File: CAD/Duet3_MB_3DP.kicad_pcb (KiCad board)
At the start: 4 copper layers, 101.9 x 125 mm, 286 parts, among them J1 SWD, J16 EXPANSION, J17 ESP_DB, J19 A2543WV-5P, J2 A2543WV-2P, J22 A2543WV-2P, J27 uSD_Socket, J30 LASER/VFD, J33 A2543WV-4P, J34 A2543WV-4P, J43 USB, J46 ETHERNET, J48 SBC, J49 A2543WV-2P, J59 A2543WV-2P, J60 A2543WV-2P, J9 VIN, M1 FID, M11 MOUNTING, M12 Logo_KICAD, M15 MOUNTING, M2 FID, M3 MOUNTING, M9 MOUNTING, Q1 BC807, Q21 MMBTA06-7-F, Q22 MMBTA06-7-F, U1 SN74F125DR, U10 AOZ1284, U11 ATSAME70Q20B-ANT, U13 MCP2542, U14 TS30041, U16 KSZ8081RNACA, U17 74LVC2G125, U19 74LVC2G34, U2 SN74F125DR, U20 Optoisolator, U21 SN74F125DR, U22 SN74F125DR, U23 Optoisolator, U27 Optoisolator, U28 Optoisolator, U3 EMIF06, U4 AP7361C-33E-13, U5 RClamp0504FB, U6 SN74F125DR, U7 AP22816AKEWT, U9 74HCT365, X1 ECS-120-10-33B-CKM-TR, X2 25Mhz

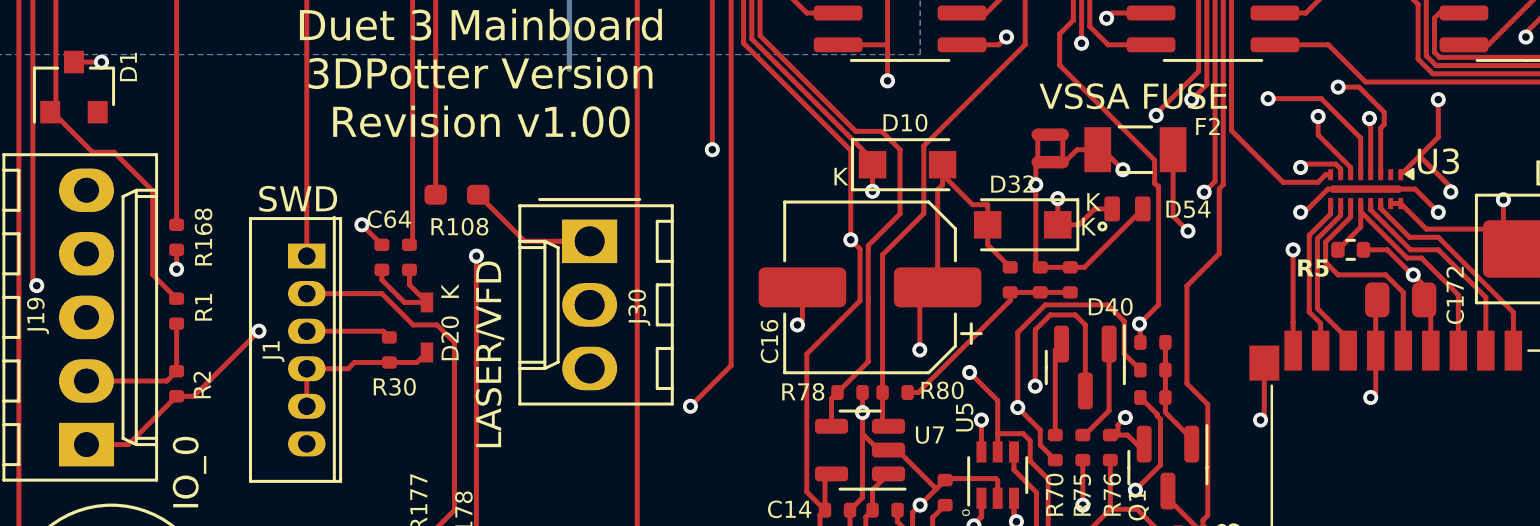
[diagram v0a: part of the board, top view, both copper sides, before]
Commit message: TODO: Finish LM5013, find replacement for TS30041
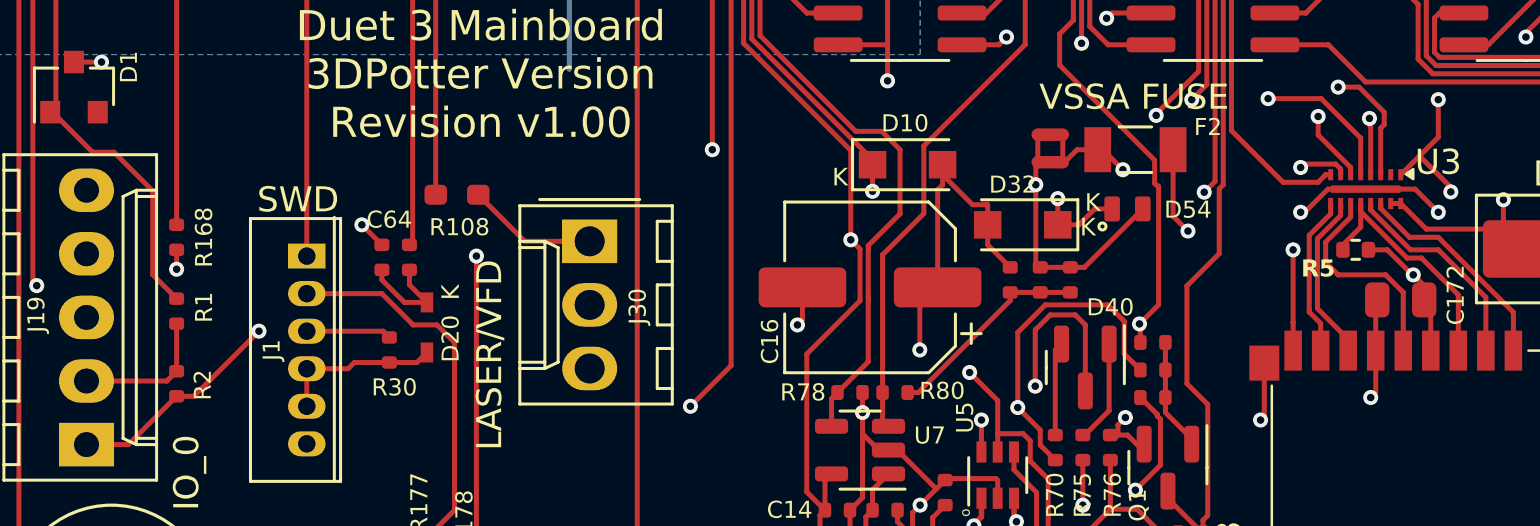
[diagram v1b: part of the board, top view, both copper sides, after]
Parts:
- moved R5 0.20 mm to (113.7, 195.0)
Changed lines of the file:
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@@
 	(footprint "Resistor_SMD:R_0402_1005Metric"
 		(layer "F.Cu")
-		(at 113.5 195)
+		(at 113.7 195)
 		(descr "Resistor SMD 0402 (1005 Metric), square (rectangular) end terminal, IPC-7351 nominal, (Body size source: IPC-SM-782 page 72, https://www.pcb-3d.com/wordpress/wp-content/uploads/ipc-sm-782a_amendment_1_and_2.pdf), generated with kicad-footprint-generator")
 		(tags "resistor")
@@
 			)
 		)
-		(property "RotOffset" "90"
+		(property "RotOffset" "270"
 			(at 0 0 180)
 			(unlocked yes)
@@
 			)
 		)
-		(property "RotOffset" "270"
+		(property "RotOffset" "90"
 			(at 0 0 180)
 			(unlocked yes)
@@
 	)
 	(segment
+		(start 116 196)
+		(end 115.96255 196)
+		(width 0.2)
+		(layer "F.Cu")
+		(net 3)
+	)
+	(segment
 		(start 159.4 183.202)
 		(end 157.102 185.5)
@@
 	)
 	(segment
-		(start 116 196)
-		(end 115.96255 196)
-		(width 0.2)
-		(layer "F.Cu")
-		(net 3)
-	)
-	(segment
 		(start 102 152)
 		(end 102.75 152.75)
@@
 	)
 	(segment
+		(start 114.96255 195)
+		(end 114.21 195)
+		(width 0.2)
+		(layer "F.Cu")
+		(net 3)
+	)
+	(segment
 		(start 122.021 144.379)
 		(end 122.021 143.1)
@@
 	)
 	(segment
+		(start 115.96255 196)
+		(end 114.96255 195)
+		(width 0.2)
+		(layer "F.Cu")
+		(net 3)
+	)
+	(segment
 		(start 66.6 200.85)
 		(end 67.2895 200.85)
@@
 	)
 	(segment
-		(start 114.96255 195)
-		(end 114.01 195)
-		(width 0.2)
-		(layer "F.Cu")
-		(net 3)
-	)
-	(segment
 		(start 106.42 145.632)
 		(end 106.395 145.607)
@@
 		(net 3)
 	)
-	(segment
-		(start 115.96255 196)
-		(end 114.96255 195)
-		(width 0.2)
-		(layer "F.Cu")
-		(net 3)
-	)
 	(via
 		(at 122.021 143.1)
@@
 	)
 	(segment
-		(start 65.6443 192.644)
-		(end 64.1 191.1)
+		(start 65.6443 195.994)
+		(end 65.6443 192.644)
 		(width 0.2)
 		(layer "F.Cu")
@@
 	)
 	(segment
-		(start 66.6 196.95)
+		(start 66.6 196.9497)
 		(end 65.6443 195.994)
 		(width 0.2)
@@
 	)
 	(segment
-		(start 65.6443 195.994)
-		(end 65.6443 192.644)
+		(start 64.1 191.1)
+		(end 63.2417 191.1)
 		(width 0.2)
 		(layer "F.Cu")
@@
 	)
 	(segment
-		(start 63.2417 191.1)
-		(end 61.6417 189.5)
+		(start 61.55 189.5)
+		(end 61.7775 189.2725)
 		(width 0.2)
 		(layer "F.Cu")
@@
 	)
 	(segment
-		(start 61.55 189.5)
-		(end 61.7775 189.2725)
+		(start 63.2417 191.1)
+		(end 61.6417 189.5)
 		(width 0.2)
 		(layer "F.Cu")
@@
 	)
 	(segment
-		(start 64.1 191.1)
-		(end 63.2417 191.1)
+		(start 66.6 196.95)
+		(end 66.6 196.9497)
 		(width 0.2)
 		(layer "F.Cu")
@@
 	)
 	(segment
+		(start 65.6443 192.644)
+		(end 64.1 191.1)
+		(width 0.2)
+		(layer "F.Cu")
+		(net 66)
+	)
+	(segment
 		(start 61.7775 164.644)
 		(end 63.9014 162.52)
@@
 	)
 	(segment
-		(start 113.9 194.09)
-		(end 112.99 195)
-		(width 0.2)
-		(layer "F.Cu")
-		(net 297)
-	)
-	(segment
 		(start 115.754412 195.328)
 		(end 113.9 193.473588)
@@
 	)
 	(segment
-		(start 113.9 193.15)
-		(end 113.9 194.09)
+		(start 113.9 194.09)
+		(end 113.19 194.8)
 		(width 0.2)
 		(layer "F.Cu")
@@
 	)
 	(segment
+		(start 113.19 194.8)
+		(end 113.19 195)
+		(width 0.2)
+		(layer "F.Cu")
+		(net 297)
+	)
+	(segment
 		(start 113.9 193.473588)
 		(end 113.9 193.15)
 		(width 0.2)
 		(layer "F.Cu")
+		(net 297)
+	)
+	(segment
+		(start 113.9 193.15)
+		(end 113.9 194.09)
+		(width 0.2)
+		(layer "F.Cu")

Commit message: Started LM70860
New 5V 6A (built for 4A) buck dc/dc converter, higher range of input voltage (4.5V-80V), built for 12V-75V according to https://webench.ti.com/power-designer/switching-regulator/customize/3?VinMin=12&VinMax=75&O1V=5&O1I=4&base_pn=LM70860-Q1&AppType=None&Flavor=None&op_TA=35&origin=pf_panel&lang_chosen=en-US&optfactor=3&Topology=Buck&flavor=None&VoltageOption=None
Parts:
- removed C146: 100uF 35V, Capacitor_SMD:CP_Elec_6.3x7.7
- removed C176: 0.1uF 50V, Capacitor_SMD:C_0603_1608Metric_Wbry
- removed C178: 10uF 50V, Capacitor_SMD:C_1206_3216Metric
- removed C182: 0.1uF 16V, Capacitor_SMD:C_0402_1005Metric_Wbry
- removed C185, C186: 22uF 25V, Capacitor_SMD:C_0805_2012Metric
- removed C187: 1uF 35V, Capacitor_SMD:C_0603_1608Metric_Wbry
- removed C206: 10nF 10V, Capacitor_SMD:C_0402_1005Metric
- removed D35: 1A,40V, Diode_SMD:D_SOD-123F
- removed J22: A2543WV-2P, Connector_Molex:Wurth_61900211121-1x02_P2.54mm_Vertical-(Molex_KK-254_AE-6410-02Acompatible)
- removed L12: 10u, Carters_Various_Bits_and_Pieces:SMD_5.2x5.7mm_1.0x2.0mm
- removed L13: 100 ohm, 4 A, Inductor_SMD:L_1206_3216Metric
- removed L2: 1uH, Inductor_SMD:L_1210_3225Metric
- removed R148: 27R, Resistor_SMD:R_0402_1005Metric_Wbry
- removed R152, R154: 60.4K, Resistor_SMD:R_0402_1005Metric_Wbry
- removed R153, R155: 4.7K, Resistor_SMD:R_0402_1005Metric_Wbry
- removed R65: 680R 0.5W, Resistor_SMD:R_0805_2012Metric
- removed U14: TS30041, Carters_Various_Bits_and_Pieces:QFN-16-1EP_3x3mm_P0.5mm_EP1.8x1.8mm
- added U24: LM70860RRXR, 3DPotter:RRX0029B-MFG, F.Cu at (94.1, 58.1)
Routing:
- net 12V_EXT: track 120.5 -> 0.00 mm, vias 1 -> 0
- net 12V_MON: track 92.3 -> 0.00 mm, vias 2 -> 0
- net /Power/12_VOUT: track 27.9 -> 0.00 mm
- net /Power/12V_VSW: track 26.2 -> 0.00 mm
- net GND: track 420.0 -> 399.6 mm, vias 87 -> 83
- net /Power/12V_VCC: track 18.5 -> 0.00 mm, vias 2 -> 0
- net V_BK_IN: track 60.6 -> 43.4 mm, vias 5 -> 4
- net /Power/12V_BST: track 7.78 -> 0.00 mm
- net VIN_POWER_MON: track 129.5 -> 123.5 mm
- net /Power/12_out: track 3.80 -> 0.00 mm
- net /Power/12V_FB: track 2.79 -> 0.00 mm
- net Net-(C182-Pad1): track 1.08 -> 0.00 mm
- removed copper zone on F.Cu, net /Power/12V_VCC
- removed copper zone on B.Cu, net GND

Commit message: PCB Layout Started
Current sensing, PG_SYNCOUT to VDDA to GND, CBOOT, Feedback are done! Fuse holder is laid out, but now we need a new power terminal, most likely changing to 250-502/000-006 from WAGO.
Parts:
- removed C136: 10nF 10V, Capacitor_SMD:C_0402_1005Metric
- removed C137, C140, C141: 10uF 50V, Capacitor_SMD:C_1206_3216Metric
- removed C138, C139, C201: 100uF 35V, Capacitor_SMD:CP_Elec_6.3x7.7
- removed C142, C203: 1nF 16V, Capacitor_SMD:C_0402_1005Metric
- removed C144, C145: 0.1uF 16V, Capacitor_SMD:C_0402_1005Metric_Wbry
- removed C147, C148, C149: 10uF 35V, Capacitor_SMD:C_1206_3216Metric
- removed D10, D31, D32: 1A,40V, Diode_SMD:D_SOD-123F
- removed D3, D9: CDBA540-HF, Diode_SMD:D_SMA
- removed D30: 3A 40V, Diode_SMD:D_SMA
- removed D37: AMBER, LED_SMD:LED_0603_1608Metric
- removed D62: 1N4148WT, complib:SOD-523F
- removed F3: PTC_3A, Fuse:Fuse_1812_4532Metric
- removed L1: 1uH, Inductor_SMD:L_1210_3225Metric
- removed L3: 8.2uH, Carters_Various_Bits_and_Pieces:SMD8x8
- removed L4: 80 Ohms @ 100MHz, Inductor_SMD:L_1206_3216Metric
- removed R102: 60.4K, Resistor_SMD:R_0402_1005Metric_Wbry
- removed R103: 4.7K, Resistor_SMD:R_0402_1005Metric_Wbry
- removed R105: 27K, Resistor_SMD:R_0402_1005Metric_Wbry
- removed R106: 37.4K, Resistor_SMD:R_0402_1005Metric_Wbry
- removed R107: 100K, Resistor_SMD:R_0402_1005Metric_Wbry
- removed R123: 15R, Resistor_SMD:R_0402_1005Metric_Wbry
- removed R124: 2.37K, Resistor_SMD:R_0402_1005Metric_Wbry
- removed R182: 820R 1%, Resistor_SMD:R_0402_1005Metric_Wbry
- removed R184: 150R, Resistor_SMD:R_0402_1005Metric_Wbry
- removed R69: 3.3K, Resistor_SMD:R_0402_1005Metric_Wbry
- removed U10: AOZ1284, complib:SO8_EP1_ThermalVias_LargeCopper
- added C21: 300pF 25V, Capacitor_SMD:C_0402_1005Metric, F.Cu at (167.1, 54.6)
- added C22: 4.7uF 100V, Capacitor_SMD:C_1210_3225Metric, F.Cu at (141.1, 44.0)
- added C23: 4.7uF 100V, Capacitor_SMD:C_1210_3225Metric, F.Cu at (141.1, 48.3)
- added C24: 4.7uF 100V, Capacitor_SMD:C_1210_3225Metric, F.Cu at (141.1, 52.5)
- added C25: 4.7uF 100V, Capacitor_SMD:C_1210_3225Metric, F.Cu at (141.1, 56.8)
- added C26: 100nF 100V, Capacitor_SMD:C_0805_2012Metric, F.Cu at (140.5, 69.6)
- added C27: 47nF 10V, Capacitor_SMD:C_0402_1005Metric, F.Cu at (103.9, 112.6)
- added C28: 47nF 16V, Capacitor_SMD:C_1210_3225Metric, F.Cu at (141.1, 61.0)
- added C29: 10nF 10V, Capacitor_SMD:C_0402_1005Metric, F.Cu at (78.9, 110.5)
- added C4: 2.2uF 10V, Capacitor_SMD:C_0603_1608Metric, F.Cu at (115.3, 119.4)
- added C5: 470nF 10V, Capacitor_SMD:C_0402_1005Metric, F.Cu at (104.1, 118.2)
- added C6: 15nF 16V, Capacitor_SMD:C_0402_1005Metric, F.Cu at (167.1, 52.6)
- added D22: CDBA5100-HF, Diode_SMD:D_SMC, F.Cu at (78.0, 101.8)
- added D25: 1A,40V, Diode_SMD:D_SOD-123F, F.Cu at (159.0, 51.3)
- added D29: 3A 40V, Diode_SMD:D_SMA, F.Cu at (163.3, 62.1)
- added D33: 1A,40V, Diode_SMD:D_SOD-123F, F.Cu at (159.0, 54.7)
- added D35: 1A,40V, Diode_SMD:D_SOD-123F, F.Cu at (159.0, 58.0)
- added F4: PTC_3A, Fuse:Fuse_1812_4532Metric, F.Cu at (165.6, 66.8)
- added F5: ~, 3DPotter:01220088Z, F.Cu at (74.2, 94.2)
- added L12: 3.9uH, Inductor_SMD:L_TDK_SLF12575, F.Cu at (119.8, 112.1)
- added L2: 1uH, Inductor_SMD:L_1210_3225Metric, F.Cu at (164.9, 71.4)
- added R38: 100k, Resistor_SMD:R_0603_1608Metric, F.Cu at (103.6, 115.8)
- added R44: 41.2K, Resistor_SMD:R_0603_1608Metric, F.Cu at (163.7, 55.9)
- added R48: 2.61k, Resistor_SMD:R_0402_1005Metric, F.Cu at (160.7, 65.3)
- added R51: 53.6K, Resistor_SMD:R_0603_1608Metric, F.Cu at (163.7, 58.4)
- added R55: 1 Ohm, Resistor_SMD:R_0402_1005Metric, F.Cu at (104.0, 113.7)
- added R60: 6 mOhm, Resistor_SMD:R_0612_1632Metric, F.Cu at (129.2, 112.0)
- added R61: 52.3k, Resistor_SMD:R_0402_1005Metric, F.Cu at (111.9, 117.8)
- added R62: 10k, Resistor_SMD:R_0402_1005Metric, F.Cu at (111.8, 116.8)
- added R63: 120K, Resistor_SMD:R_0805_2012Metric, F.Cu at (76.8, 108.1)
- added R64: 4.7K, Resistor_SMD:R_0402_1005Metric, F.Cu at (79.0, 109.5)
- F1: value VIN_FUSE -> ~; footprint Fuse:FuseHolder_Blade_ATO_Littelfuse_FLR_178.6165 -> 3DPotter:01220088Z
- F12: value FUSE 30V 300mA-500mA -> FUSE 90V 300mA-500mA; footprint Fuse:Fuse_BelFuse_OZCG_1812 -> Fuse:Fuse_1210_3225Metric
- R16: value 10.7K -> 35.7K; footprint Resistor_SMD:R_0402_1005Metric -> Resistor_SMD:R_0603_1608Metric
- moved U24 56.8 mm to (108.4, 113.1)
- moved J2 23.9 mm to (74.7, 122.7)
- moved J9 23.3 mm to (118.3, 81.0)
- moved F1 4.97 mm to (100.8, 94.2)
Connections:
- F1 pad 1: V_FUSED -> V_IN
- U24 pad 1: unconnected-(U24-VIN4-Pad1) -> /Power/VIN1
- U24 pad 11: unconnected-(U24-ISNS+-Pad11) -> /Power/ISNS+
- U24 pad 12: unconnected-(U24-VOUT-Pad12) -> /Power/5V_Common
- U24 pad 13: unconnected-(U24-CONFIG-Pad13) -> /Power/CONFIG
- U24 pad 14: unconnected-(U24-RT-Pad14) -> /Power/RT
- U24 pad 15: unconnected-(U24-EXTCOMP-Pad15) -> /Power/EXTCOMP
- U24 pad 16: unconnected-(U24-FB-Pad16) -> /Power/FB
- U24 pad 17: unconnected-(U24-AGND-Pad17) -> GND
- U24 pad 18: unconnected-(U24-VDDA-Pad18) -> /Power/VDDA
- U24 pad 19: unconnected-(U24-VCC-Pad19) -> /Power/CAP_VCC
- U24 pad 2: unconnected-(U24-VIN5-Pad2) -> /Power/VIN1
- U24 pad 20: unconnected-(U24-SW1-Pad20) -> /Power/SW
- U24 pad 21: unconnected-(U24-SW2-Pad21) -> /Power/SW
- U24 pad 22: unconnected-(U24-SW3-Pad22) -> /Power/SW
- U24 pad 23: unconnected-(U24-PGND1-Pad23) -> GND
- U24 pad 24: unconnected-(U24-PGND2-Pad24) -> GND
- U24 pad 25: unconnected-(U24-PGND3-Pad25) -> GND
- U24 pad 26: unconnected-(U24-PGND4-Pad26) -> GND
- U24 pad 27: unconnected-(U24-VIN1-Pad27) -> /Power/VIN1
- U24 pad 28: unconnected-(U24-VIN2-Pad28) -> /Power/VIN1
- U24 pad 29: unconnected-(U24-VIN3-Pad29) -> /Power/VIN1
- U24 pad 3: unconnected-(U24-VIN6-Pad3) -> /Power/VIN1
- U24 pad 30: unconnected-(U24-PGND-Pad30) -> GND
- U24 pad 4: unconnected-(U24-CBOOT-Pad4) -> /Power/CBOOT
- U24 pad 5: unconnected-(U24-SW4-Pad5) -> /Power/SW4
- U24 pad 6: unconnected-(U24-BIAS-Pad6) -> /Power/5V_Common
- U24 pad 7: unconnected-(U24-PG_SYNCOUT-Pad7) -> /Power/PG_SYNCOUT
- U24 pad 8: unconnected-(U24-PFM_SYNCIN-Pad8) -> GND
- U24 pad 9: unconnected-(U24-EN_UVLO-Pad9) -> /Power/VIN1
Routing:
- net 5V_EXT: track 184.5 -> 109.8 mm, vias 2 -> 1
- net /Power/5V_Common: track 0.00 -> 59.6 mm, vias 0 -> 5
- net V_FUSED: track 189.8 -> 130.5 mm, vias 4 -> 3
- net V_FUSED_IO: track 58.5 -> 13.1 mm, vias 1 -> 0
- net V_BK_IN: track 43.4 -> 0.00 mm, vias 4 -> 0
- net /Power/5V_common: track 32.8 -> 0.00 mm, vias 4 -> 0
- net /Power/5VIN_BUCK_IN: track 28.5 -> 0.00 mm
- net /Power/ISNS+: track 0.00 -> 26.6 mm, vias 0 -> 2
- net GND: track 399.6 -> 380.7 mm, vias 83 -> 73
- net VIN_POWER_MON: track 123.5 -> 107.3 mm
- net /Power/VDDA: track 0.00 -> 15.2 mm, vias 0 -> 2
- net /Power/5VIN_BUCK_EN: track 14.7 -> 0.00 mm, vias 2 -> 0
- net (no net): track 0.00 -> 14.0 mm, vias 0 -> 4
- net /Power/5VIN_BUCK_FSW: track 12.8 -> 0.00 mm, vias 2 -> 0
- net /Power/5VIN_BUCK_FB: track 11.3 -> 0.00 mm
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- added copper zone on F.Cu, net /Power/ISNS+
- added copper zone on F.Cu, net /Power/SW
- removed copper zone on B.Cu, net /Power/5VIN_BUCK_IN
- removed copper zone on F.Cu, net /Power/L3_OUT
- removed copper zone on F.Cu, net /Power/LX
- removed copper zone on B.Cu, net V_FUSED
- removed copper zone on B.Cu, net V_IN
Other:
- board text removed: "-"
- board text removed: "V_IN"

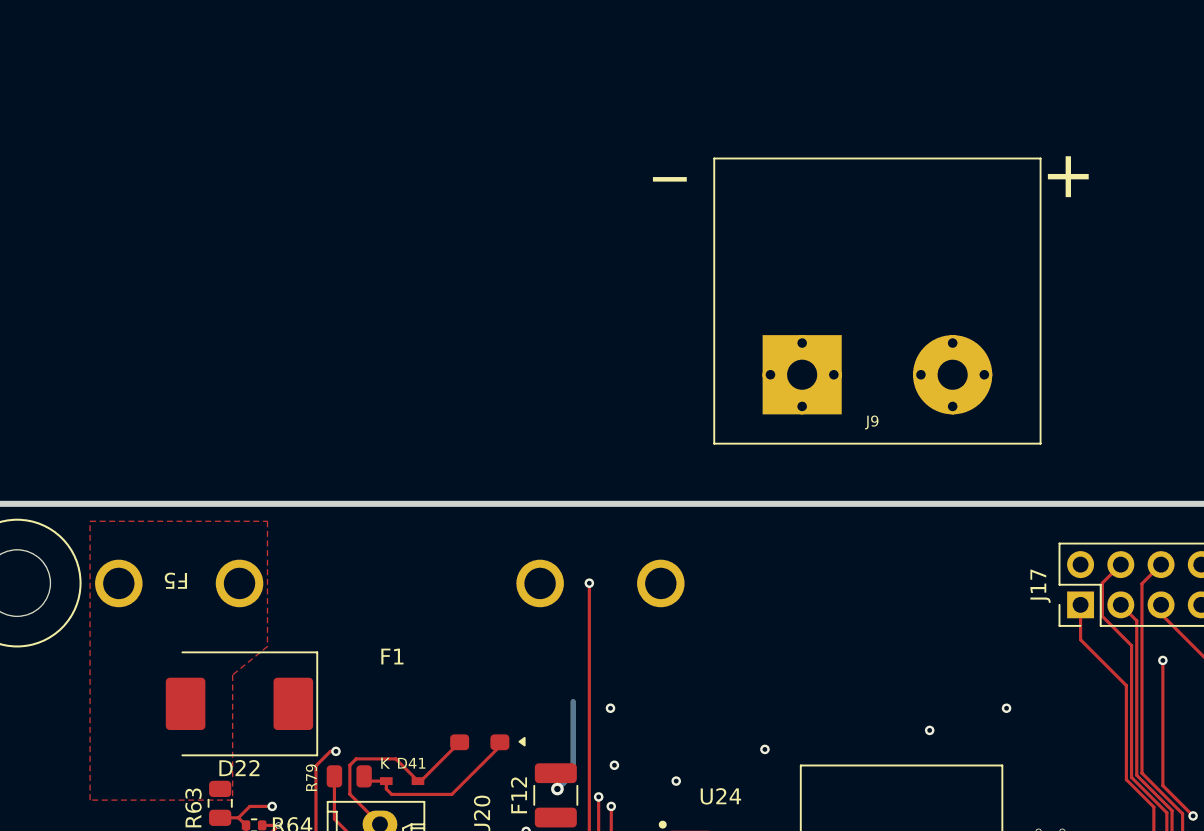
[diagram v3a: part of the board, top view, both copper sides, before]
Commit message: New VIN Connector added
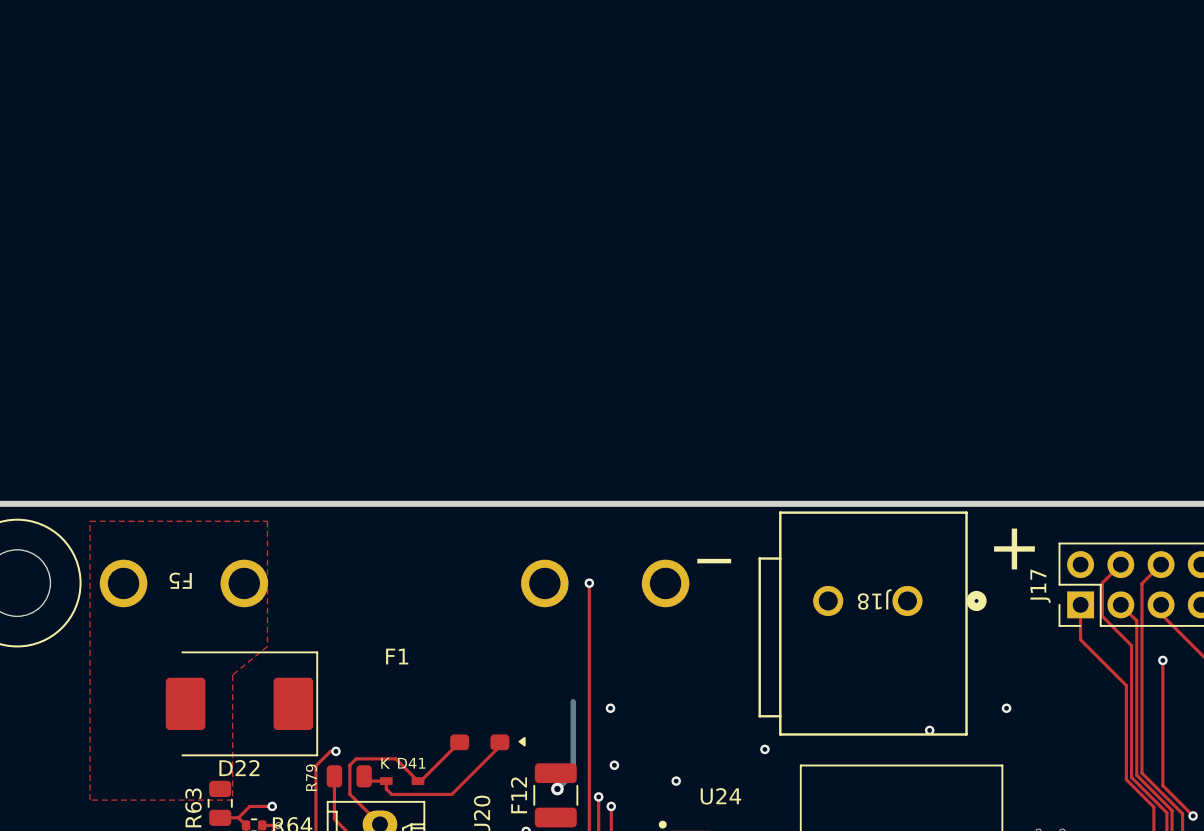
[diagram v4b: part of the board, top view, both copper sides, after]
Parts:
- removed J9: VIN, complib:screwt-barrier-9.5mm-1x2
- added J18: 250-502/000-006, 3DPotter:CONN2_250-502&slash_000-006_WAG, F.Cu at (120.2, 95.3)
- moved F5 0.30 mm to (74.5, 94.2)
- moved F1 0.30 mm to (101.1, 94.2)
